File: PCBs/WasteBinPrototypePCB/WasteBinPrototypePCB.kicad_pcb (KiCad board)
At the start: 2 copper layers, 31 parts, among them J1 Jack-DC 12V, J2 Conn_01x10_Male, J3 Conn_01x06_Male, J4 SM04B-SRSS-TB(LF)(SN), Q1 MMBT3904, Q2 IRL540NSTRLPBF, U1 PC817, U2 TLV1117-50, U3 ESP32-C3-DEVKITC-02, U4 A1301EUA-T

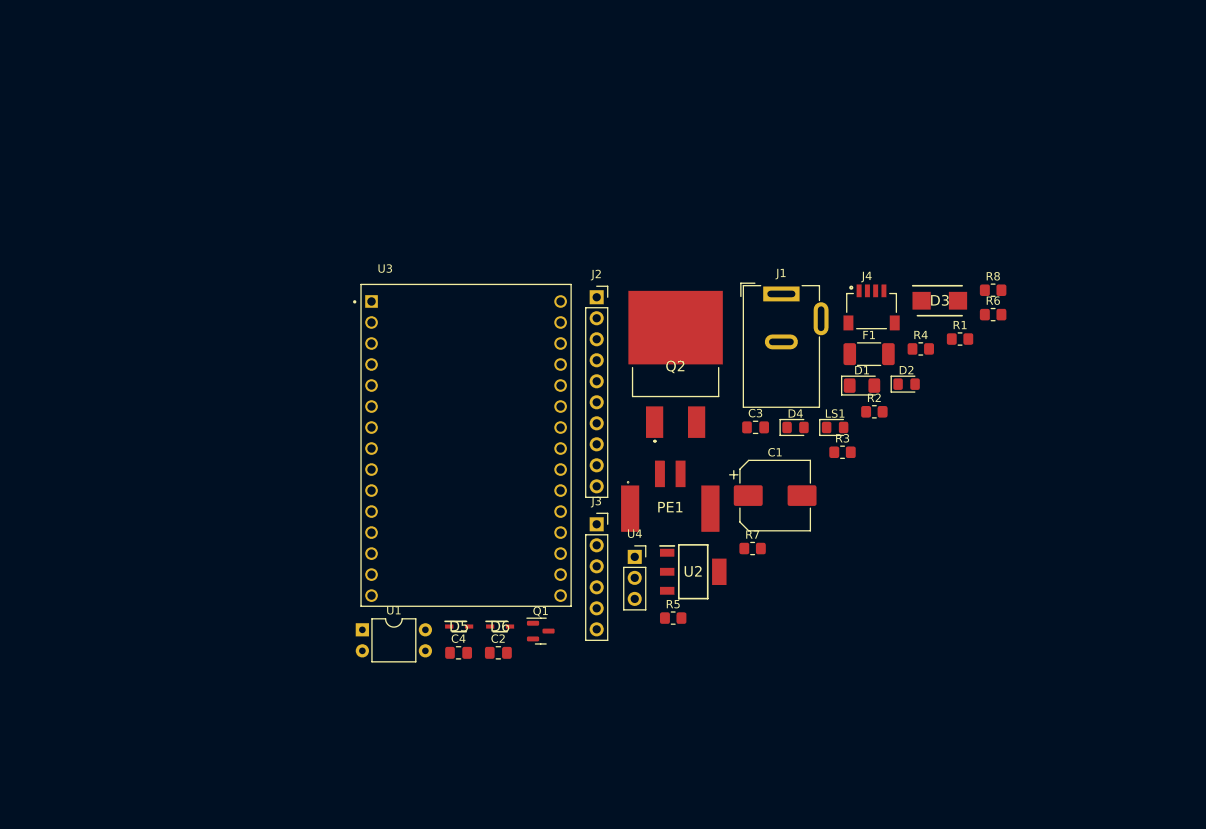
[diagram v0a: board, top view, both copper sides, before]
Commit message: grouped componentes
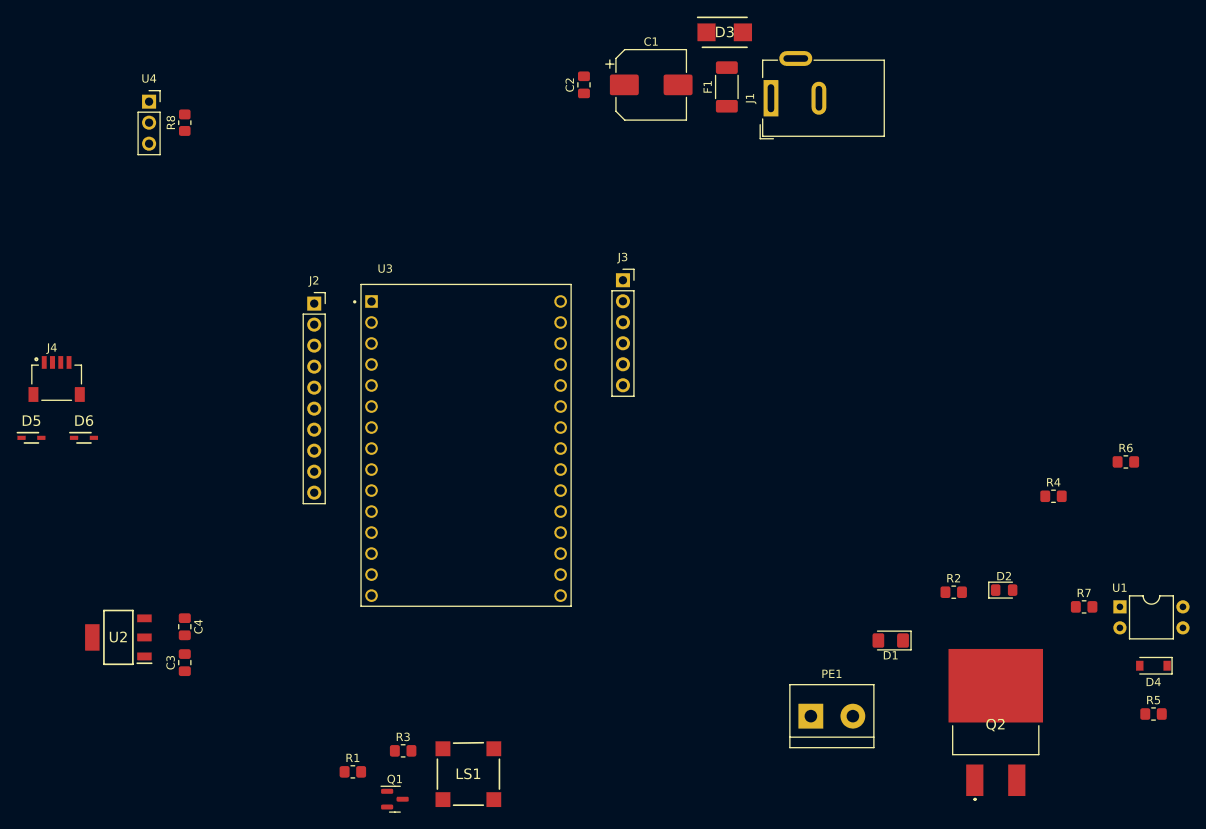
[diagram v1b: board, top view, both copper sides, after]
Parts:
- D4: value D -> 1N4148W; footprint Diode_SMD:D_0805_2012Metric_Pad1.15x1.40mm_HandSolder -> Diode_SMD:D_SOD-123
- LS1: footprint LED_SMD:LED_0805_2012Metric_Pad1.15x1.40mm_HandSolder -> SamacSys_Parts:CMT752580SMTTR
- PE1: footprint SamacSys_Parts:1808190 -> TerminalBlock:TerminalBlock_bornier-2_P5.08mm
- moved R8 99.8 mm to (83.8, 59.7), turned to 90 degrees
- moved J4 98.9 mm to (68.3, 88.7)
- moved U1 91.6 mm to (196.9, 118.2)
- moved R1 90.2 mm to (104.1, 138.2)
- moved U4 80.5 mm to (79.5, 57.1)
- moved C3 74.6 mm to (83.8, 125.0), turned to 90 degrees
- moved U2 70.0 mm to (75.8, 121.9), turned to 180 degrees
- moved C2 69.4 mm to (132.1, 55.1), turned to 90 degrees
- moved R3 64.2 mm to (110.2, 135.6)
- moved LS1 61.0 mm to (118.1, 138.4)
- moved R5 59.2 mm to (200.9, 131.2)
- moved Q2 58.1 mm to (181.9, 134.4)
- moved D5 56.5 mm to (65.3, 97.8)
- moved D6 55.2 mm to (71.6, 97.8)
- moved D4 52.0 mm to (200.9, 125.3), turned to 180 degrees
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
